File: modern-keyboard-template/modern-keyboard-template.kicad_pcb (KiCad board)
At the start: 4 copper layers, 65.9 x 43.9 mm, 25 parts, among them J1 USB_C_Receptacle_USB2.0, J2 Conn_01x05, U1 STM32F072CBT6, U2 PRTR5V0U2X, U3 XC6206PxxxMR-Regulator_Linear, U5 TXB0101

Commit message: Updates
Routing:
- net GND: track 166.1 -> 167.6 mm, vias 8 -> 5
- net +3V3: track 105.5 -> 104.8 mm
- added copper zone on F.Cu, net +5V
- added copper zone on B.Cu, net GND
- removed copper zone on In1.Cu, net +5V
- removed copper zone on In2.Cu, net GND
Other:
- copper layers 4 -> 2

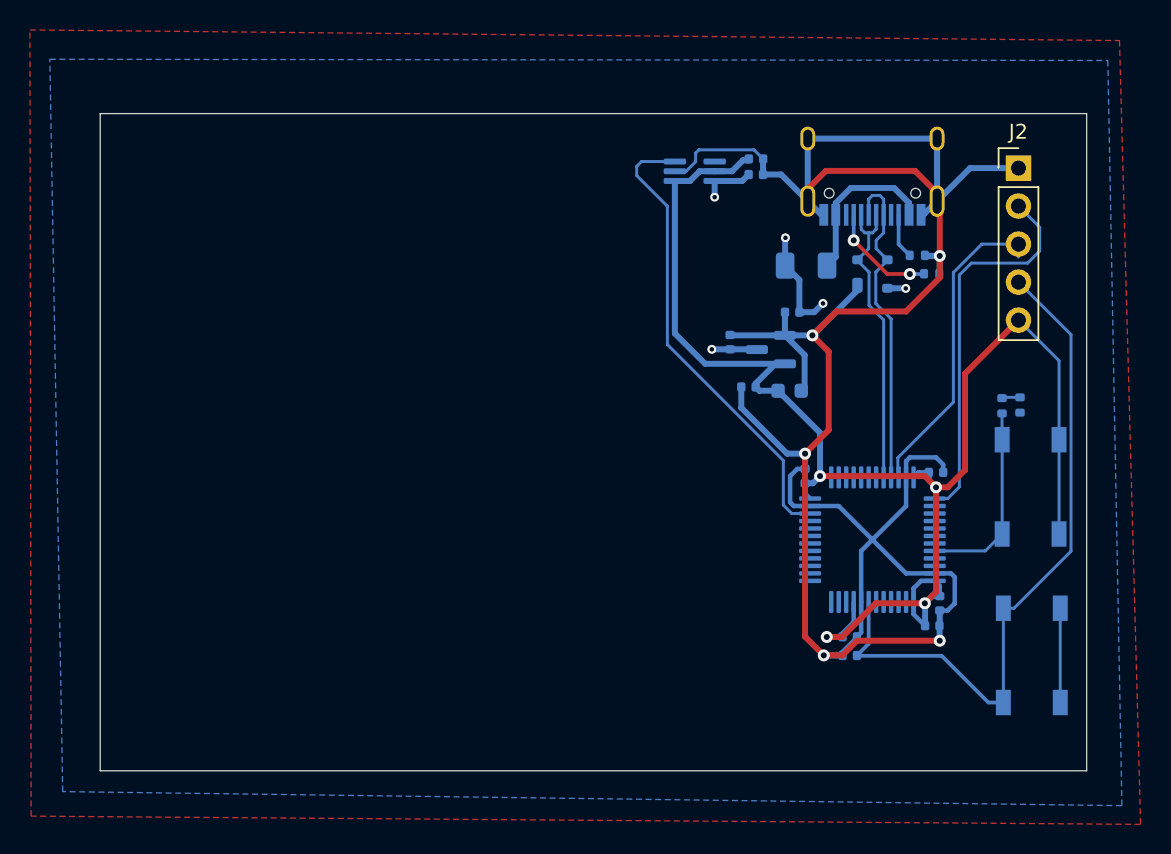
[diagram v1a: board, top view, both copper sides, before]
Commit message: Added PCBWay DRC presets
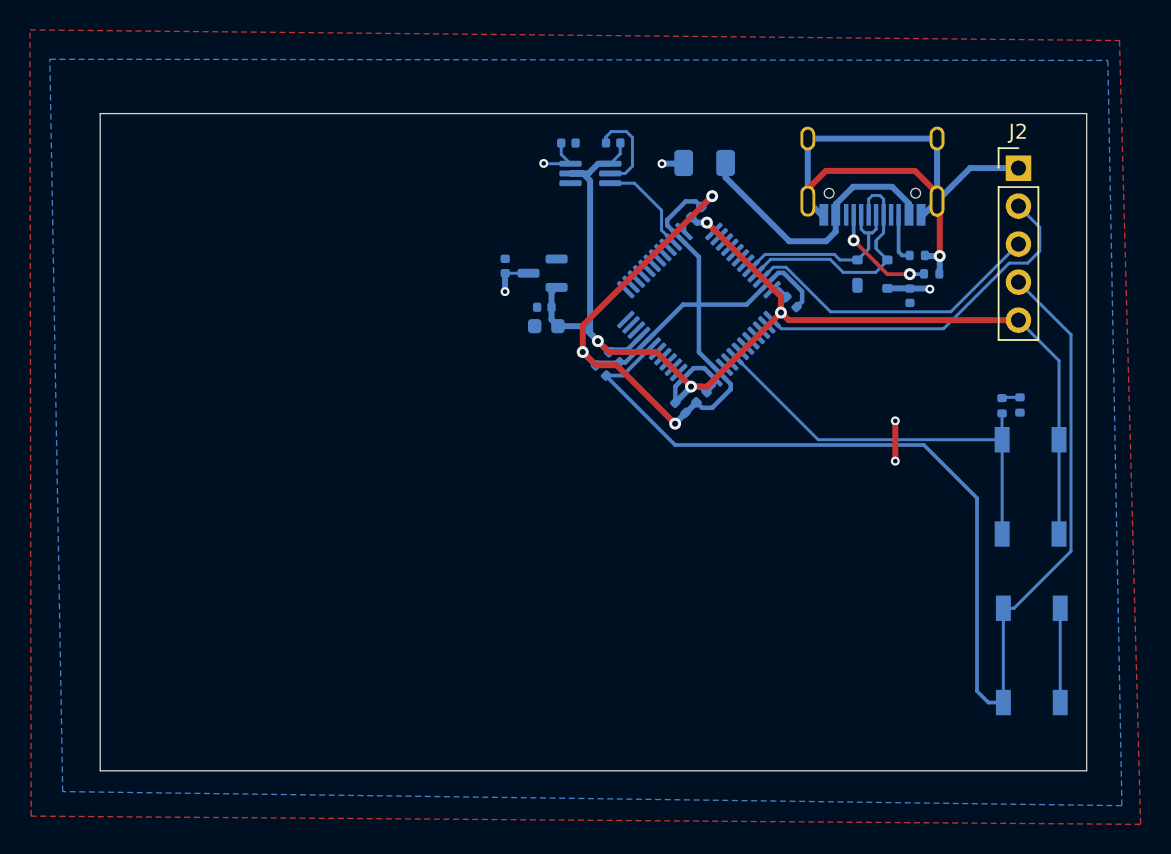
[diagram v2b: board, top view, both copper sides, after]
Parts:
- moved C1 25.3 mm to (178.4, 55.4), turned to 135 degrees
- moved C7 24.4 mm to (179.3, 54.5), turned to -45 degrees
- moved C6 22.3 mm to (183.7, 57.9), turned to -45 degrees
- moved C5 21.0 mm to (185.1, 57.2), turned to -135 degrees
- moved U1 19.5 mm to (184.9, 51.0), turned to 45 degrees
- moved C4 19.1 mm to (184.8, 44.8), turned to 45 degrees
- moved C2 16.8 mm to (174.7, 52.5), turned to 180 degrees
- moved U3 16.1 mm to (174.5, 48.9)
- moved C9 15.9 mm to (172.0, 48.4)
- moved C3 14.9 mm to (191.1, 50.8), turned to -45 degrees
- moved C10 14.6 mm to (174.6, 51.2)
- moved C44 12.7 mm to (176.2, 40.2)
- moved F1 9.64 mm to (185.3, 41.6)
- moved C43 9.60 mm to (179.2, 40.2), turned to 0 degrees
- moved C8 7.95 mm to (199.0, 50.4), turned to -90 degrees
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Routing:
- net GND: track 167.6 -> 122.6 mm, vias 5 -> 6
- net NRST: track 46.8 -> 78.9 mm
- net RGB3.3: track 31.4 -> 6.62 mm
- net BOOT0: track 13.0 -> 28.2 mm
- net +3V3: track 104.8 -> 95.5 mm
- net VBUS: track 10.9 -> 18.8 mm
- net D-: track 20.4 -> 13.9 mm
- net D+: track 22.1 -> 17.2 mm
- net +5V: track 15.0 -> 10.3 mm, vias 5 -> 4
- net SWCLK: track 25.7 -> 23.9 mm

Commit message: Fixed capacitor orientation
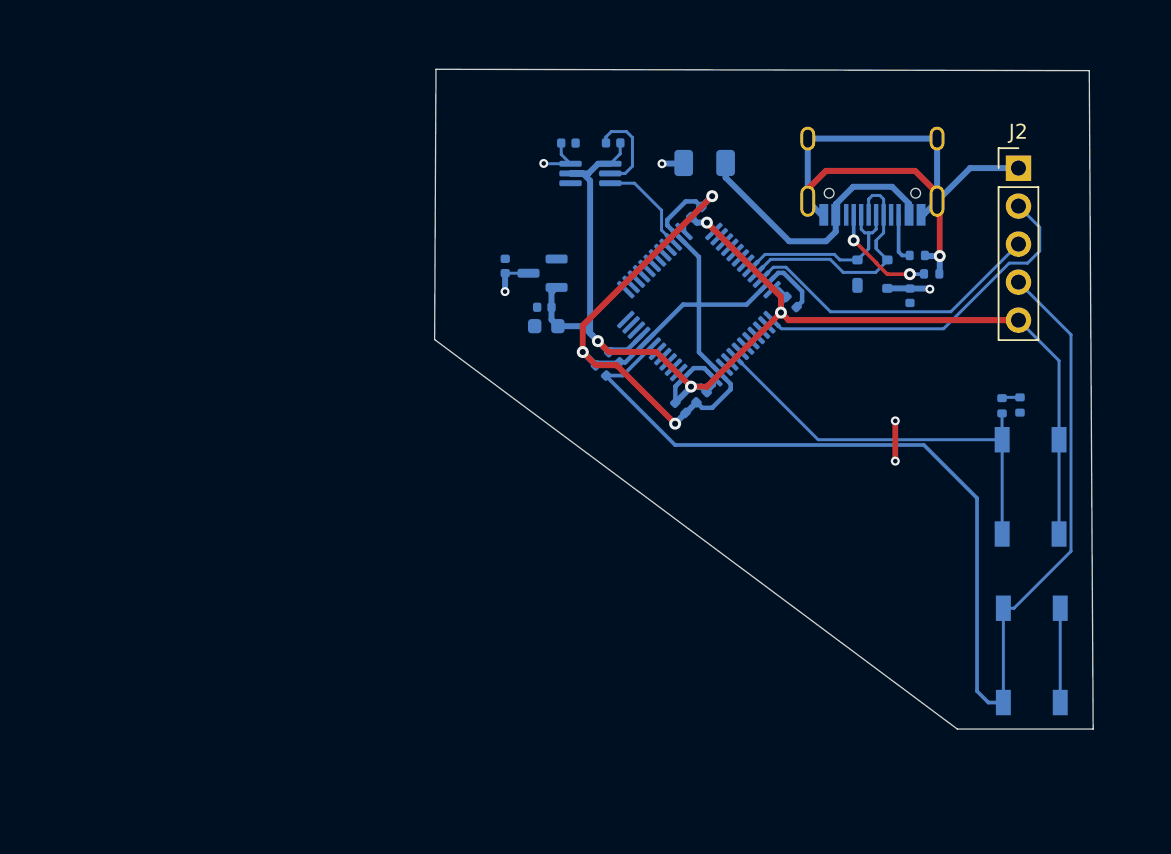
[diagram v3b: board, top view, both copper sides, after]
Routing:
- removed copper zone on F.Cu, net +5V
- removed copper zone on B.Cu, net GND
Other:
- board size 65.9 x 43.9 mm -> 44 x 44.1 mm
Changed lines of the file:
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@@
 		(allow_soldermask_bridges_in_footprints no)
 		(pcbplotparams
-			(layerselection 0x00010fc_ffffffff)
-			(plot_on_all_layers_selection 0x0000000_00000000)
+			(layerselection 0x0000000_7fffffff)
+			(plot_on_all_layers_selection 0x000c100_80000000)
 			(disableapertmacros no)
 			(usegerberextensions no)
@@
 			(plotfptext yes)
 			(plotinvisibletext no)
-			(sketchpadsonfab no)
+			(sketchpadsonfab yes)
 			(subtractmaskfromsilk no)
-			(outputformat 1)
+			(outputformat 5)
 			(mirror no)
-			(drillshape 1)
+			(drillshape 0)
 			(scaleselection 1)
-			(outputdirectory "")
+			(outputdirectory "/Users/charliesteenhagen/Desktop/")
 		)
 	)
@@
 		)
 		(property "JlcRotOffset" ""
-			(at 210.2925 55.4925 360)
+			(at 210.2925 55.4925 0)
 			(layer "B.Fab")
 			(hide yes)
@@
 		)
 		(property "LCSC" "C307331"
-			(at 210.2925 55.4925 360)
+			(at 210.2925 55.4925 0)
 			(layer "B.Fab")
 			(hide yes)
@@
 		(tags "SOT-143")
 		(property "Reference" "U2"
-			(at -6.43 -4.0675 360)
+			(at -6.43 -4.0675 0)
 			(layer "B.SilkS")
 			(effects
@@
 		)
 		(property "Value" "PRTR5V0U2X"
-			(at -5.14 0.19 360)
+			(at -5.14 0.19 0)
 			(layer "B.Fab")
 			(hide yes)
@@
 		)
 		(property "Footprint" "Package_TO_SOT_SMD:SOT-143"
-			(at 0 0 360)
+			(at 0 0 0)
 			(layer "B.Fab")
 			(hide yes)
@@
 		)
 		(property "Datasheet" "https://assets.nexperia.com/documents/data-sheet/PRTR5V0U2X.pdf"
-			(at 0 0 360)
+			(at 0 0 0)
 			(layer "B.Fab")
 			(hide yes)
@@
 		)
 		(property "Description" ""
-			(at 0 0 360)
+			(at 0 0 0)
 			(layer "B.Fab")
 			(hide yes)
@@
 		)
 		(property "JlcRotOffset" "90"
-			(at 271.785 -148.3 360)
+			(at 271.785 -148.3 0)
 			(layer "B.Fab")
 			(hide yes)
@@
 		)
 		(property "LCSC" "C2827688"
-			(at 271.785 -148.3 360)
+			(at 271.785 -148.3 0)
 			(layer "B.Fab")
 			(hide yes)
@@
 		(tags "resistor")
 		(property "Reference" "R1"
-			(at -1.88 -0.02 360)
+			(at -1.88 -0.02 0)
 			(layer "B.SilkS")
 			(effects
@@
 		)
 		(property "Value" "5.1k"
-			(at -2.1 -1.38 360)
+			(at -2.1 -1.38 0)
 			(layer "B.Fab")
 			(effects
@@
 		)
 		(property "Footprint" "Resistor_SMD:R_0402_1005Metric"
-			(at 0 0 360)
+			(at 0 0 0)
 			(layer "B.Fab")
 			(hide yes)
@@
 		)
 		(property "Datasheet" ""
-			(at 0 0 360)
+			(at 0 0 0)
 			(layer "B.Fab")
 			(hide yes)
@@
 		)
 		(property "Description" ""
-			(at 0 0 360)
+			(at 0 0 0)
 			(layer "B.Fab")
 			(hide yes)
@@
 		)
 		(fp_text user "${REFERENCE}"
-			(at 0 0 360)
+			(at 0 0 0)
 			(layer "B.Fab")
 			(effects
@@
 		(tags "fuse")
 		(property "Reference" "F1"
-			(at -3.15 0.54 360)
+			(at -3.15 0.54 0)
 			(layer "B.SilkS")
 			(effects
@@
 		)
 		(property "Value" "500mA"
-			(at -0.16 1.37 360)
+			(at -0.16 1.37 0)
 			(layer "B.Fab")
 			(effects
@@
 		)
 		(property "Footprint" "Fuse:Fuse_1206_3216Metric"
-			(at 0 0 360)
+			(at 0 0 0)
 			(layer "B.Fab")
 			(hide yes)
@@
 		)
 		(property "Datasheet" ""
-			(at 0 0 360)
+			(at 0 0 0)
 			(layer "B.Fab")
 			(hide yes)
@@
 		)
 		(property "Description" ""
-			(at 0 0 360)
+			(at 0 0 0)
 			(layer "B.Fab")
 			(hide yes)
@@
 		)
 		(property "LCSC" "C135341"
-			(at 271.785 -156.8 360)
+			(at 271.785 -156.8 0)
 			(layer "B.Fab")
 			(hide yes)
@@
 		)
 		(fp_text user "${REFERENCE}"
-			(at 0 0 360)
+			(at 0 0 0)
 			(layer "B.Fab")
 			(effects
@@
 		(tags "resistor")
 		(property "Reference" "R2"
-			(at 2.89036 -0.07036 360)
+			(at 2.89036 -0.07036 0)
 			(layer "B.SilkS")
 			(effects
@@
 		)
 		(property "Value" "5.1k"
-			(at 3.46 -1.32 360)
+			(at 3.46 -1.32 0)
 			(layer "B.Fab")
 			(effects
@@
 		)
 		(property "Footprint" "Resistor_SMD:R_0402_1005Metric"
-			(at 0 0 360)
+			(at 0 0 0)
 			(layer "B.Fab")
 			(hide yes)
@@
 		)
 		(property "Datasheet" ""
-			(at 0 0 360)
+			(at 0 0 0)
 			(layer "B.Fab")
 			(hide yes)
@@
 		)
 		(property "Description" ""
-			(at 0 0 360)
+			(at 0 0 0)
 			(layer "B.Fab")
 			(hide yes)
@@
 		)
 		(fp_text user "${REFERENCE}"
-			(at 0 0 360)
+			(at 0 0 0)
 			(layer "B.Fab")
 			(effects
@@
 		)
 	)
-	(gr_rect
-		(start 144.925 38.26)
-		(end 210.835 82.17)
+	(gr_line
+		(start 202.19 79.38)
+		(end 167.27 53.36)
+		(stroke
+			(width 0.05)
+			(type default)
+		)
+		(layer "Edge.Cuts")
+	)
+	(gr_line
+		(start 167.27 53.36)
+		(end 167.36 35.3)
+		(stroke
+			(width 0.05)
+			(type default)
+		)
+		(layer "Edge.Cuts")
+	)
+	(gr_line
+		(start 167.36 35.3)
+		(end 211.01 35.39)
+		(stroke
+			(width 0.05)
+			(type default)
+		)
+		(layer "Edge.Cuts")
+	)
+	(gr_line
+		(start 211.01 35.39)
+		(end 211.27 79.38)
+		(stroke
+			(width 0.05)
+			(type default)
+		)
+		(layer "Edge.Cuts")
+	)
+	(gr_line
+		(start 211.27 79.38)
+		(end 202.19 79.38)
 		(stroke
 			(width 0.05)
 			(type default)
 		)
-		(fill none)
 		(layer "Edge.Cuts")
 	)
@@
 		(net 21)
 	)
-	(zone
-		(net 5)
-		(net_name "+5V")
-		(layer "F.Cu")
-		(hatch edge 0.5)
-		(priority 1)
-		(connect_pads
-			(clearance 0.5)
-		)
-		(min_thickness 0.25)
-		(filled_areas_thickness no)
-		(fill yes
-			(thermal_gap 0.5)
-			(thermal_bridge_width 0.5)
-		)
-		(polygon
-			(pts
-				(xy 140.23 32.67) (xy 213.03 33.38) (xy 214.44 85.75) (xy 140.31 85.2)
-			)
-		)
-	)
-	(zone
-		(net 4)
-		(net_name "GND")
-		(layer "B.Cu")
-		(hatch edge 0.5)
-		(connect_pads
-			(clearance 0.5)
-		)
-		(min_thickness 0.25)
-		(filled_areas_thickness no)
-		(fill yes
-			(thermal_gap 0.5)
-			(thermal_bridge_width 0.5)
-		)
-		(polygon
-			(pts
-				(xy 141.56 34.63) (xy 212.25 34.71) (xy 213.19 84.5) (xy 142.42 83.56)
-			)
-		)
-	)
 )
